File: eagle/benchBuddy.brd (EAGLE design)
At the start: 100 x 80 mm, 74 parts, among them IC2 TLC274D, IC3 LM334Z, IC4 LM324D, IC5 LM324D, J1 12V_DC, Q1 600mA/40V, U1 LP2983AIM5-1.0/NOPB, U2 LP2985-10DBVR

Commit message: Added all parts. Schematic finished. Consider Rev 1.0
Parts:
- added C10, C12, C14, C9: 10uF, rcl:C0805
- added C11, C8: 0.1uF, rcl:C0805
- added D1, D2, D3: (no value), SparkFun-LED:LED_3MM
- added F1: 4A It, lab07lib:LITTELFUSE_MINISMDC260F/12-2
- added F2, F3: 1.5A It, lab07lib:LITTELFUSE_MINISMDC260F/12-2
- added J4, J8: GND, lab07lib:FAT-PAD
- added J5: 3.3V, lab07lib:FAT-PAD
- added J6: 5V, lab07lib:FAT-PAD
- added J7: 12V, lab07lib:FAT-PAD
- added J9: 0-10V, lab07lib:FAT-PAD
- added PS1, PS2: P78E05-1000, P78E05-1000:CONV_P78E05-1000
- added R31, R32, R33: (no value), rcl:R1206
- added U3: 3V3REG, PowerManagementParts:SOT223
- renumbered JP3 to J3, U$3 to J2
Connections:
- new net 3.3V: C10.1, C11.1, D3.A, J5.P$1, U3.2, U3.4
- new net 5V: C8.1, C9.1, D2.A, J3.6, J6.P$1, PS2.3
- new net N$4: D1.A
- new net N$41: D1.K, R31.2
- new net N$42: D2.K, R32.2
- new net N$43: D3.K, R33.2
- new net N$44: F1.2, U$2.COM
- new net N$45: IC4.7, LED3.A
- new net N$46: IC4.8, LED4.A
- new net N$47: IC4.14, LED5.A
- new net N$48: F2.1, PS1.3
- new net N$49: C12.1, F2.2, U3.3
- new net N$7: F3.2, PS2.1
- net 10VOLTS: no longer J3.6
- net GND: now also C10.2, C11.2, C12.2, C14.2, C8.2, C9.2, J4.P$1, J8.P$1, PS1.2, PS2.2, R31.1, R32.1, R33.1, U3.1
- net N$3: now also F1.1; no longer U$2.COM
- net VCC: now also J9.P$1
- net VIN: now also C14.1, F3.1, J7.P$1, PS1.1

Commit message: Basic dimensions and mechanical layout of board
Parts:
- removed U$2: EG2362, lab07lib:SWITCH_EG2362-ND
- added SW4: EG2362, lab07lib:SWITCH_EG2362-ND
- moved J4 380.6 mm to (68.6, 6.35)
- moved J5 374.1 mm to (76.2, 6.35)
- moved J6 367.7 mm to (83.8, 6.35)
- moved J7 361.4 mm to (91.4, 6.35)
- moved J8 355.1 mm to (99.1, 6.35)
- moved J9 348.9 mm to (106.7, 6.35)
- moved D1 255.4 mm to (91.4, 16.5)
- moved D2 253.3 mm to (83.8, 16.5)
- moved D3 251.2 mm to (76.2, 16.5)
- moved C10 244.4 mm to (52.1, -74.9)
- moved C11 244.4 mm to (52.1, -80.0)
- moved C12 244.4 mm to (52.1, -85.1)
- moved C14 244.4 mm to (52.1, -96.5)
- moved C8 244.4 mm to (52.1, -64.8)
- moved C9 244.4 mm to (52.1, -69.8)
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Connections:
- removed net N$4: D1.A
- net N$44: now also SW4.COM; no longer U$2.COM
- net ON1: now also SW4.ON1; no longer U$2.ON1
- net VIN: now also D1.A, SW4.ON2; no longer U$2.ON2
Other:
- board size 100 x 80 mm -> 126.7 x 76.2 mm

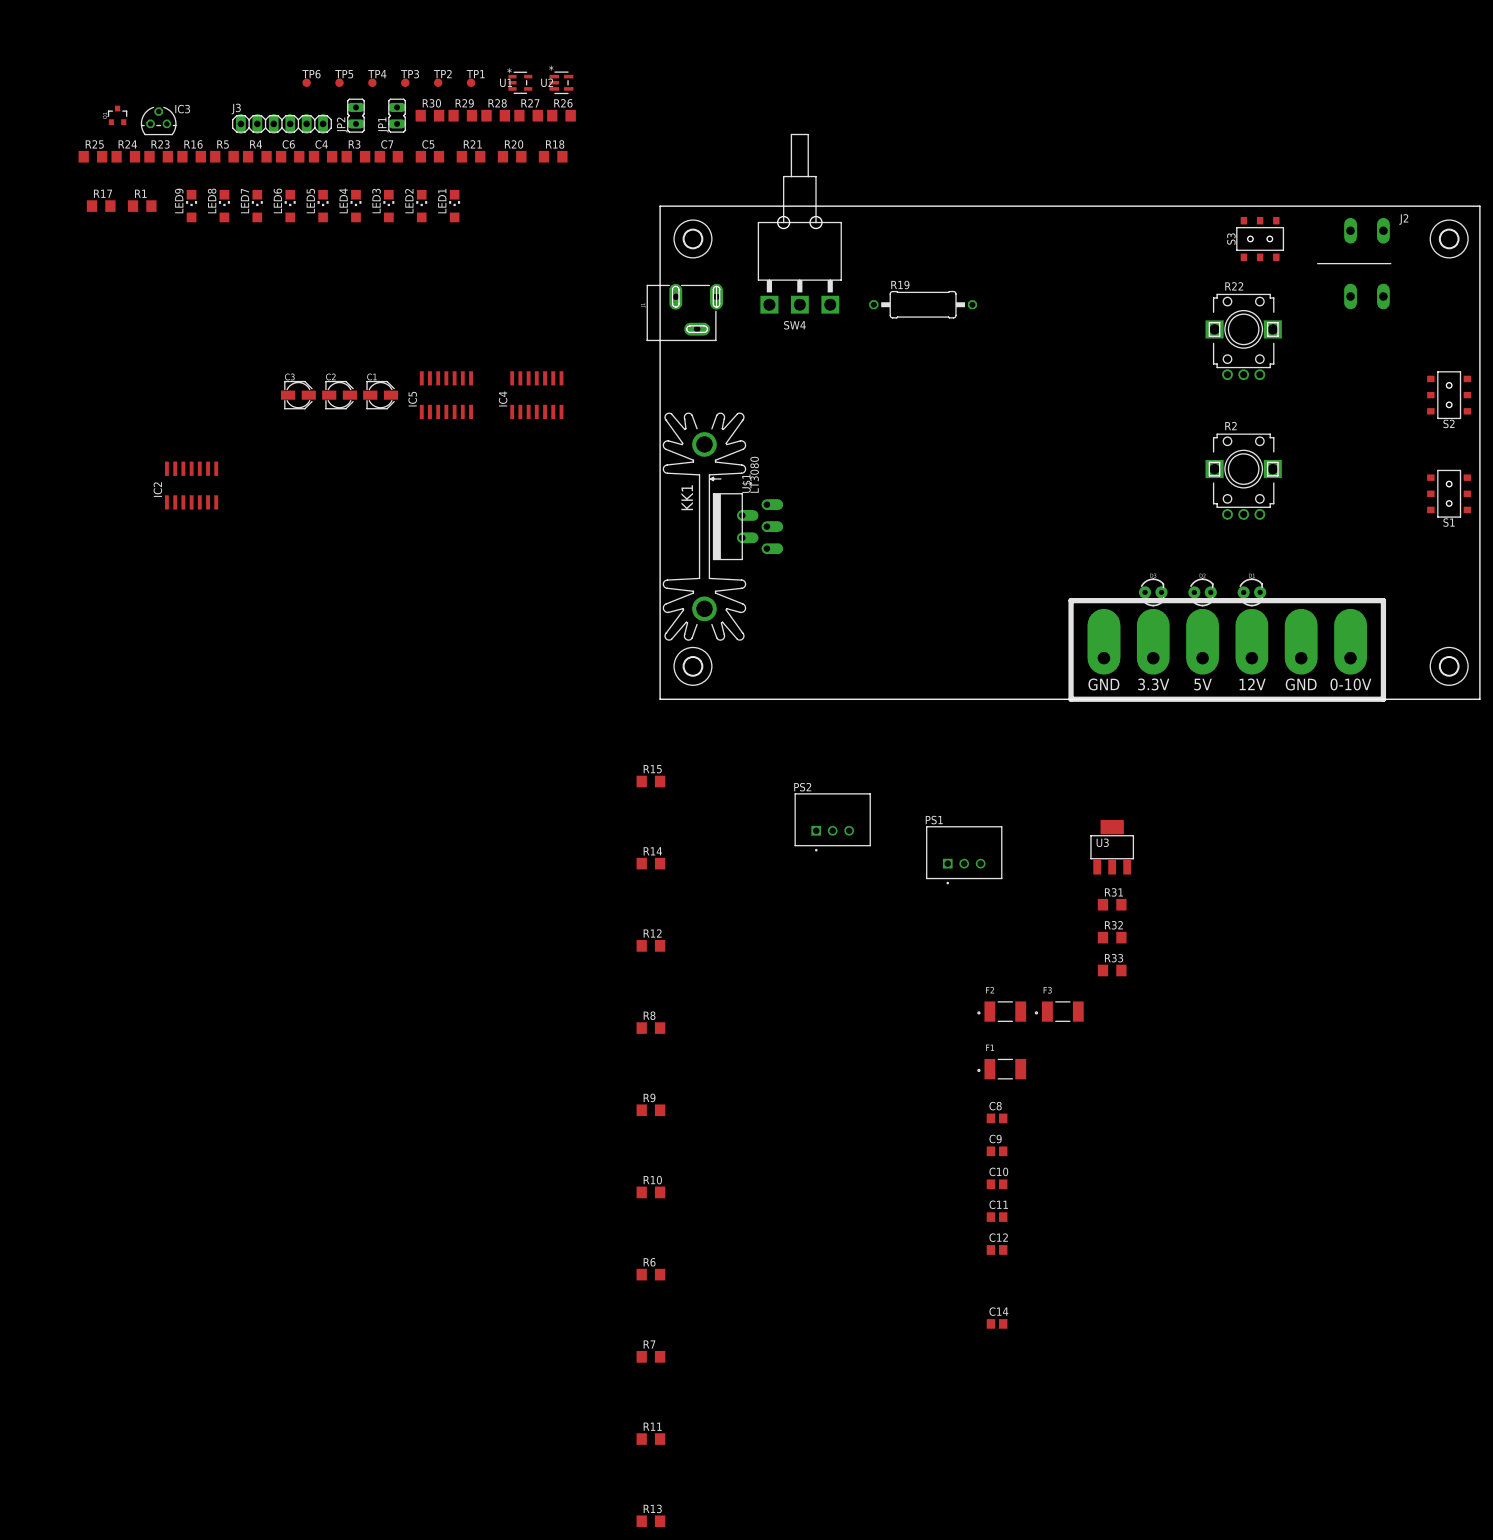
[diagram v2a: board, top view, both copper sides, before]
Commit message: More detailed board layout. Began LED and VU layout
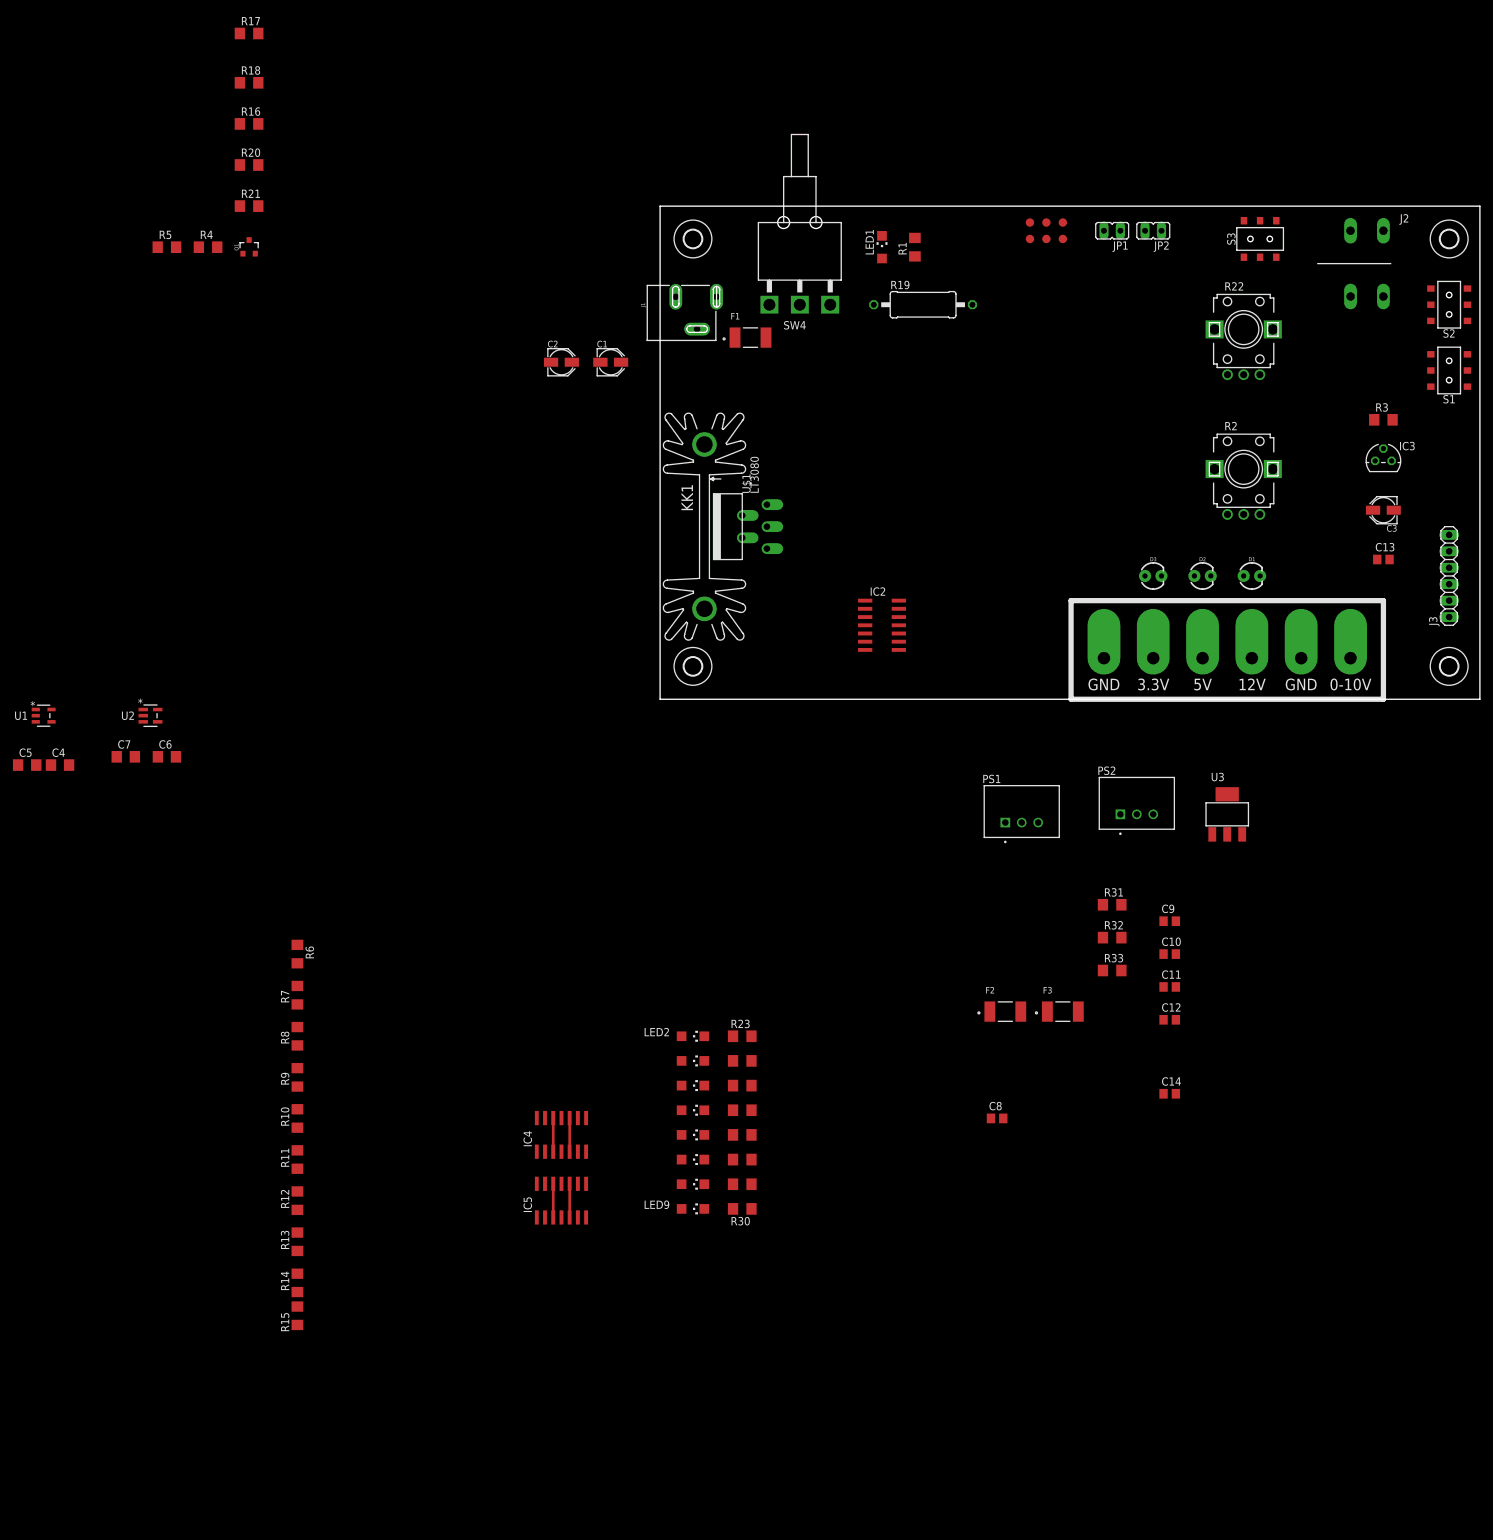
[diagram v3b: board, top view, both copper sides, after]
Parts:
- added C13: 0.1uF, rcl:C0805
- moved IC3 196.3 mm to (111.8, 36.8)
- moved J3 193.4 mm to (121.9, 19.1), turned to 90 degrees
- moved R30 175.7 mm to (12.7, -78.7)
- moved R25 175.1 mm to (12.7, -59.7)
- moved LED9 173.2 mm to (5.08, -78.7), turned to 270 degrees
- moved R29 170.7 mm to (12.7, -74.9)
- moved R24 169.1 mm to (12.7, -55.9)
- moved C3 168.6 mm to (111.8, 29.2), turned to 180 degrees
- moved LED8 167.6 mm to (5.08, -74.9), turned to 270 degrees
- moved R28 165.7 mm to (12.7, -71.1)
- moved R3 163.9 mm to (111.8, 43.2)
- moved R23 163.1 mm to (12.7, -52.1)
- moved LED7 162.0 mm to (5.08, -71.1), turned to 270 degrees
- moved R27 160.9 mm to (12.7, -67.3)
- moved LED6 156.4 mm to (5.08, -67.3), turned to 270 degrees
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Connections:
- removed net N$22: C7.1, U2.5
- removed net N$37: C5.1, U1.5
- net 10VOLTS: now also C7.1, U2.5
- net 1VOLT: now also C5.1, U1.5
- net GND: now also C13.2
- net VCC: now also C13.1
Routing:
- net DISPLAY: track 0.00 -> 20.8 mm

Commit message: Most components in final position
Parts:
- moved R14 176.2 mm to (66.0, 36.8)
- moved R15 176.2 mm to (66.0, 31.8)
- moved R13 175.2 mm to (66.0, 41.9)
- moved R12 174.3 mm to (66.0, 47.0)
- moved IC4 154.3 mm to (82.5, 52.1)
- moved R11 153.0 mm to (58.4, 30.5)
- moved R10 152.2 mm to (58.4, 35.6)
- moved R9 151.4 mm to (58.4, 40.6)
- moved R8 150.5 mm to (58.4, 45.7)
- moved R7 149.7 mm to (58.4, 50.8)
- moved R6 148.9 mm to (58.4, 55.9), turned to 90 degrees
- moved IC5 146.6 mm to (82.5, 31.8)
- moved R5 142.1 mm to (53.3, 11.4), turned to 270 degrees
- moved LED8 138.7 mm to (95.2, 30.5)
- moved R29 138.7 mm to (102.9, 30.5)
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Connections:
- net 10VOLTS: now also J3.6
- net 5V: no longer J3.6
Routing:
- net GND: track 0.00 -> 31.3 mm
- added copper zone on layer 1, net VIN

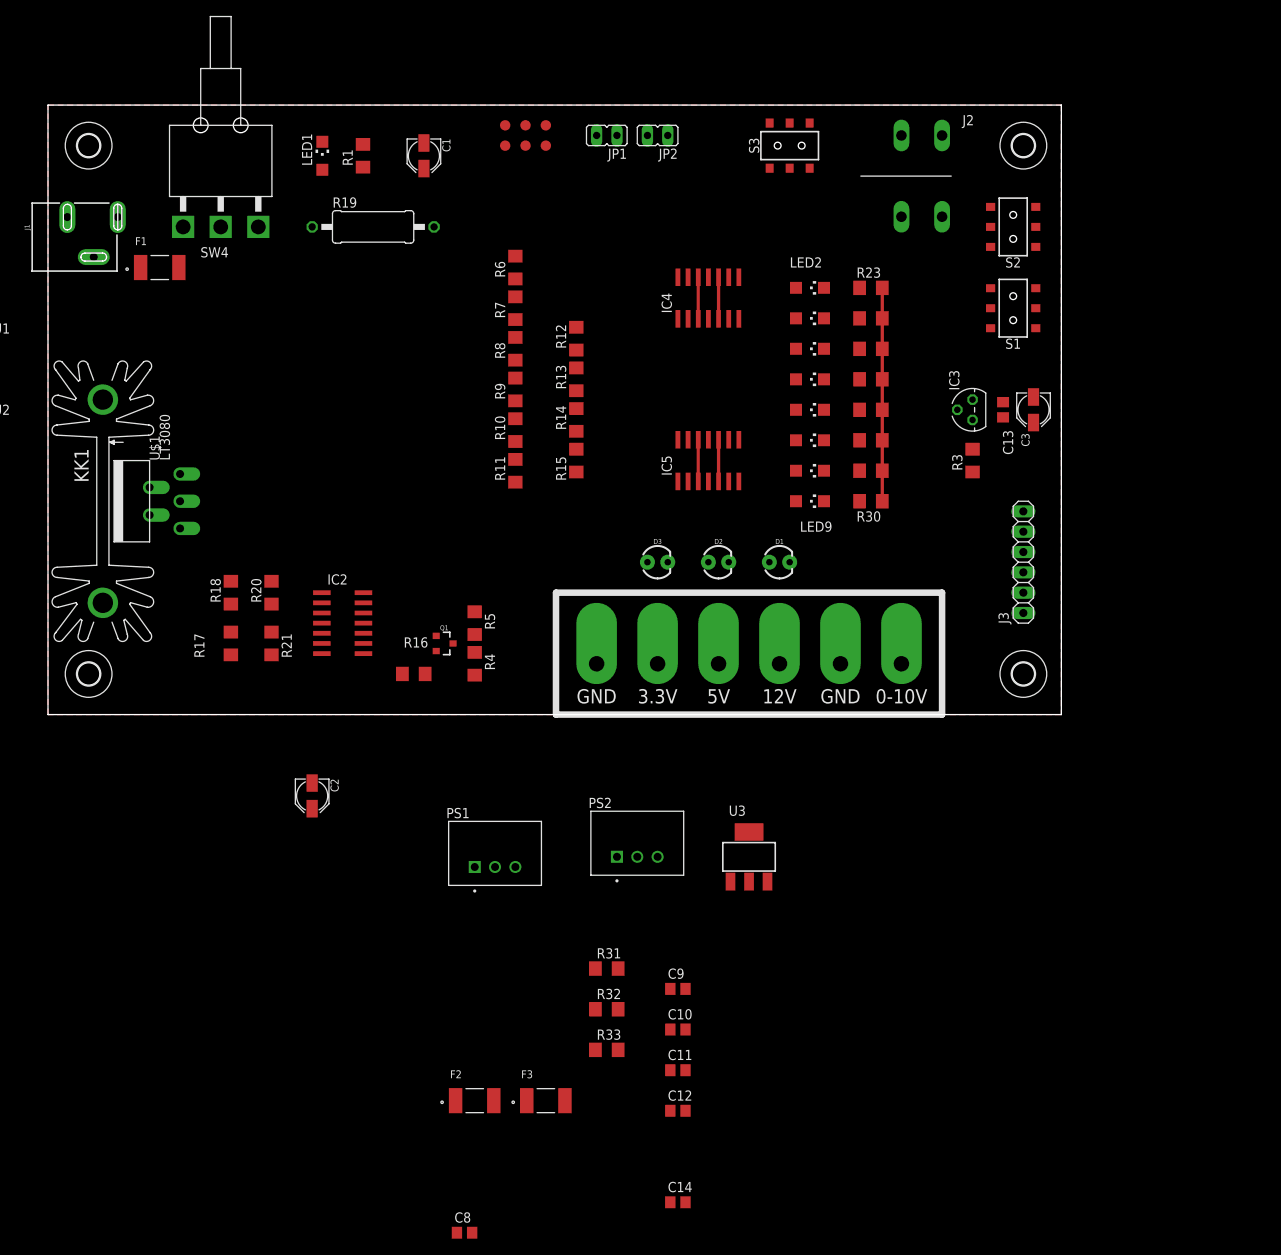
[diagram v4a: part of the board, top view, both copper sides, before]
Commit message: VU meter routed
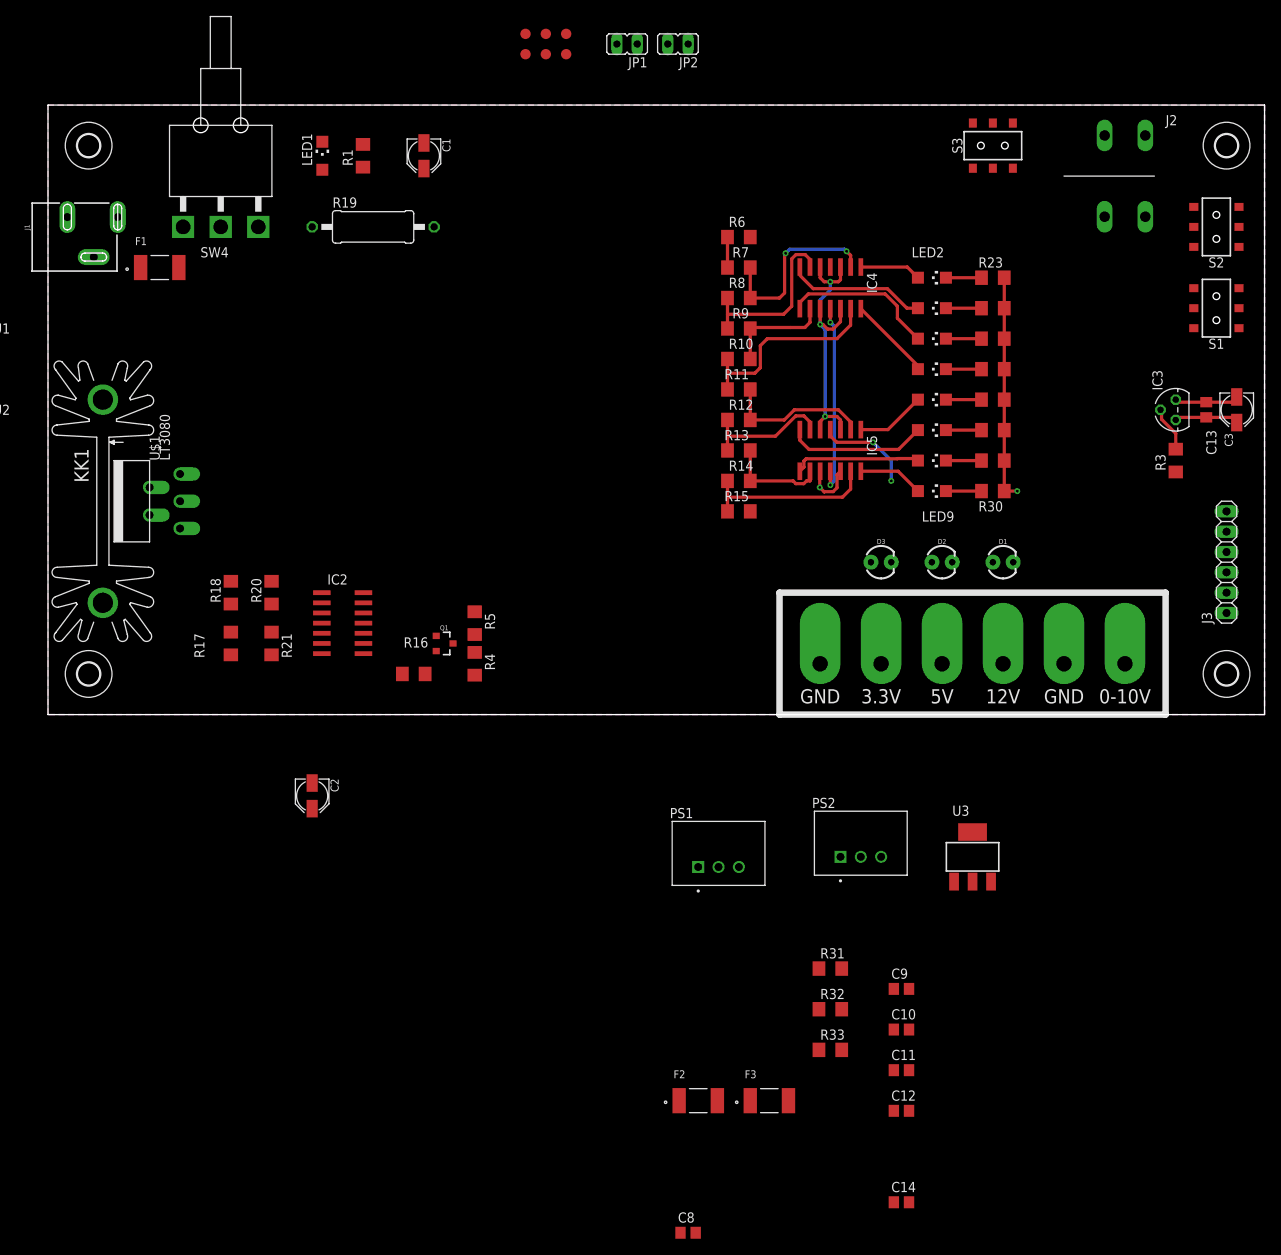
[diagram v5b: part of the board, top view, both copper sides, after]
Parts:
- moved R11 29.7 mm to (86.4, 40.6), turned to 180 degrees
- moved R10 29.3 mm to (86.4, 44.5), turned to 0 degrees
- moved R9 29.0 mm to (86.4, 48.3), turned to 180 degrees
- moved R8 28.7 mm to (86.4, 52.1), turned to 0 degrees
- moved R7 28.4 mm to (86.4, 55.9), turned to 180 degrees
- moved R6 28.2 mm to (86.4, 59.7), turned to 0 degrees
- moved C10 27.9 mm to (106.7, -39.4)
- moved C11 27.9 mm to (106.7, -44.5)
- moved C12 27.9 mm to (106.7, -49.5)
- moved C14 27.9 mm to (106.7, -61.0)
- moved C9 27.9 mm to (106.7, -34.3)
- moved D2 27.9 mm to (111.8, 19.1)
- moved J6 27.9 mm to (111.8, 6.35)
- moved R31 27.9 mm to (97.8, -31.8)
- moved R32 27.9 mm to (97.8, -36.8)
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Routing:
- net GND: track 31.3 -> 65.1 mm, vias 0 -> 3
- net N$16: track 0.00 -> 25.4 mm
- net N$13: track 0.00 -> 23.5 mm, vias 0 -> 2
- net N$14: track 0.00 -> 21.9 mm
- net N$9: track 0.00 -> 21.8 mm
- net DISPLAY: track 20.8 -> 42.5 mm, vias 0 -> 4
- net N$46: track 0.00 -> 19.2 mm
- net HALF_LADDER: track 0.00 -> 18.5 mm
- net N$34: track 0.00 -> 17.6 mm
- net N$11: track 0.00 -> 16.4 mm
- net N$45: track 0.00 -> 16.4 mm
- net N$35: track 0.00 -> 16.0 mm
- net N$15: track 0.00 -> 13.3 mm
- net N$10: track 0.00 -> 12.8 mm
- net VIN: track 0.00 -> 12.2 mm, vias 0 -> 2
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- added copper zone on layer 16, net GND
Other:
- board size 126.7 x 76.2 mm -> 152.1 x 76.2 mm
